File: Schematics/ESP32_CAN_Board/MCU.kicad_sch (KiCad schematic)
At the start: 8 parts, among them U4 ESP32-C3-MINI-1-N4

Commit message: initial design completed
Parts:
- added J1, J2: Screw_Terminal_01x04, TerminalBlock:TerminalBlock_Xinya_XY308-2.54-4P_1x04_P2.54mm_Horizontal, symbol Connector:Screw_Terminal_01x04
- added J3: Screw_Terminal_01x02, TerminalBlock:TerminalBlock_Xinya_XY308-2.54-2P_1x02_P2.54mm_Horizontal, symbol Connector:Screw_Terminal_01x02
- U4: footprint ESP32-C3-MINI-1-N4:XCVR_ESP32-C3-MINI-1-N4 -> myFootprints:XCVR_ESP32-C3-MINI-1-N4
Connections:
- net ESPPower is gone; now on net +3.3V: C1.1, C2.1, U4.3 (3V3)
- net Pin12: now reaches U4.12 (IO0)
- net Pin12: now also J2.2 (Pin_2)
- net Pin13: now reaches U4.13 (IO1)
- net Pin13: now also J2.3 (Pin_3)
- net Pin16: now reaches U4.16 (IO10)
- net Pin16: now also J2.4 (Pin_4)
- net Pin18: now reaches U4.18 (IO4)
- net Pin18: now also J1.1 (Pin_1)
- net at U4.21 (IO7): now also J1.2 (Pin_2)
- net at U4.22 (IO8): now also J1.3 (Pin_3)
- net at U4.23 (IO9): now also J1.4 (Pin_4)
- net at U4.30 (RXD0): now also J3.2 (Pin_2)
- net at U4.31 (TXD0): now also J3.1 (Pin_1)
- net Pin6: now reaches U4.6 (IO3)
- net Pin6: now also J2.1 (Pin_1)
- no-connect marks 12 -> 4
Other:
- moved on the sheet: C1, C2

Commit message: finished ready for order
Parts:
- J1, J2: LCSC (none) -> C915913
- J3: LCSC (none) -> C557685
- R5: LCSC C96346 -> C84376
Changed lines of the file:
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@@
+			)
+		)
+		(property "LCSC" "C915913"
+			(at 95.25 78.74 0)
+			(hide yes)
+			(show_name no)
+			(do_not_autoplace no)
+			(effects
+				(font
+					(size 1.27 1.27)
+				)
 			)
 		)
@@
 			)
 		)
+		(property "LCSC" "C915913"
+			(at 204.47 88.9 0)
+			(hide yes)
+			(show_name no)
+			(do_not_autoplace no)
+			(effects
+				(font
+					(size 1.27 1.27)
+				)
+			)
+		)
 		(pin "2"
 		)
@@
 			)
 		)
-		(property "LCSC" "C96346"
+		(property "LCSC" "C84376"
 			(at 44.45 116.84 90)
 			(hide yes)
@@
 			(at 97.79 109.22 0)
 			(hide yes)
+			(show_name no)
+			(do_not_autoplace no)
+			(effects
+				(font
+					(size 1.27 1.27)
+				)
+			)
+		)
+		(property "LCSC" " C557685"
+			(at 97.79 109.22 0)
+			(hide yes)

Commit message: mcu schematic update
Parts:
- added PowerLED1: RLED, LED_SMD:LED_0603_1608Metric_Pad1.05x0.95mm_HandSolder, symbol Device:LED
- added R7: 1k, Resistor_SMD:R_0805_2012Metric_Pad1.20x1.40mm_HandSolder, symbol Device:R
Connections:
- net +3.3V: now also R7.2
- net GND: now also PowerLED1.1 (K)
- new net: PowerLED1.2 (A), R7.1

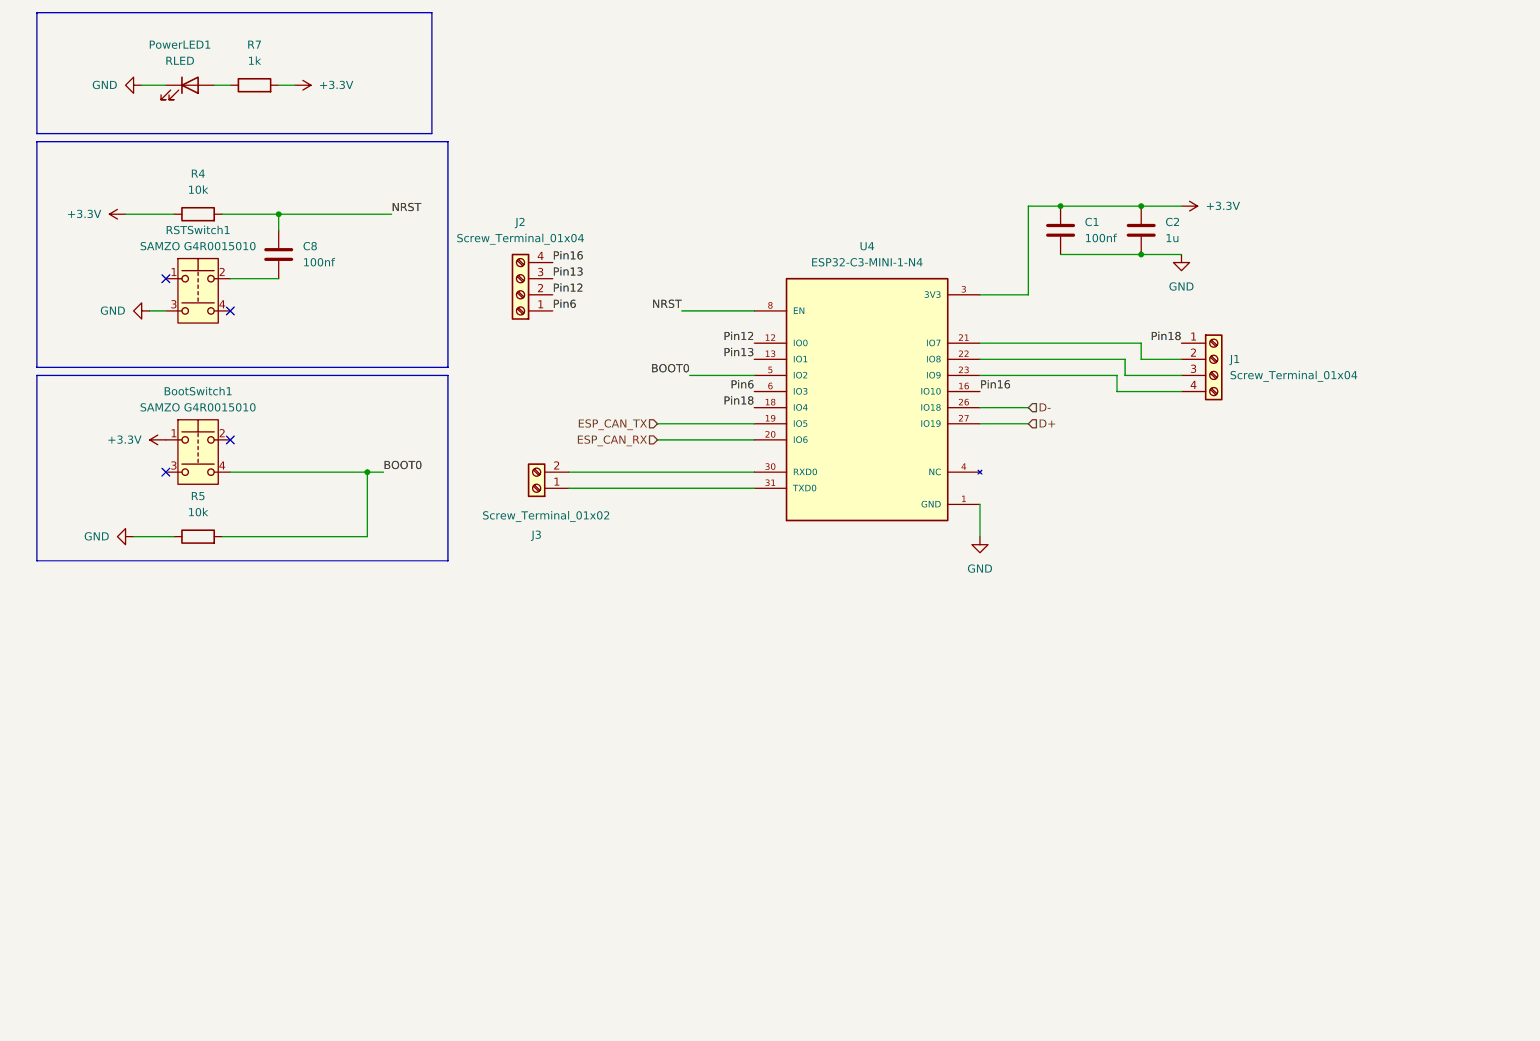
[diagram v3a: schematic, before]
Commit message: final Draft Completed, In JLPCB Cart
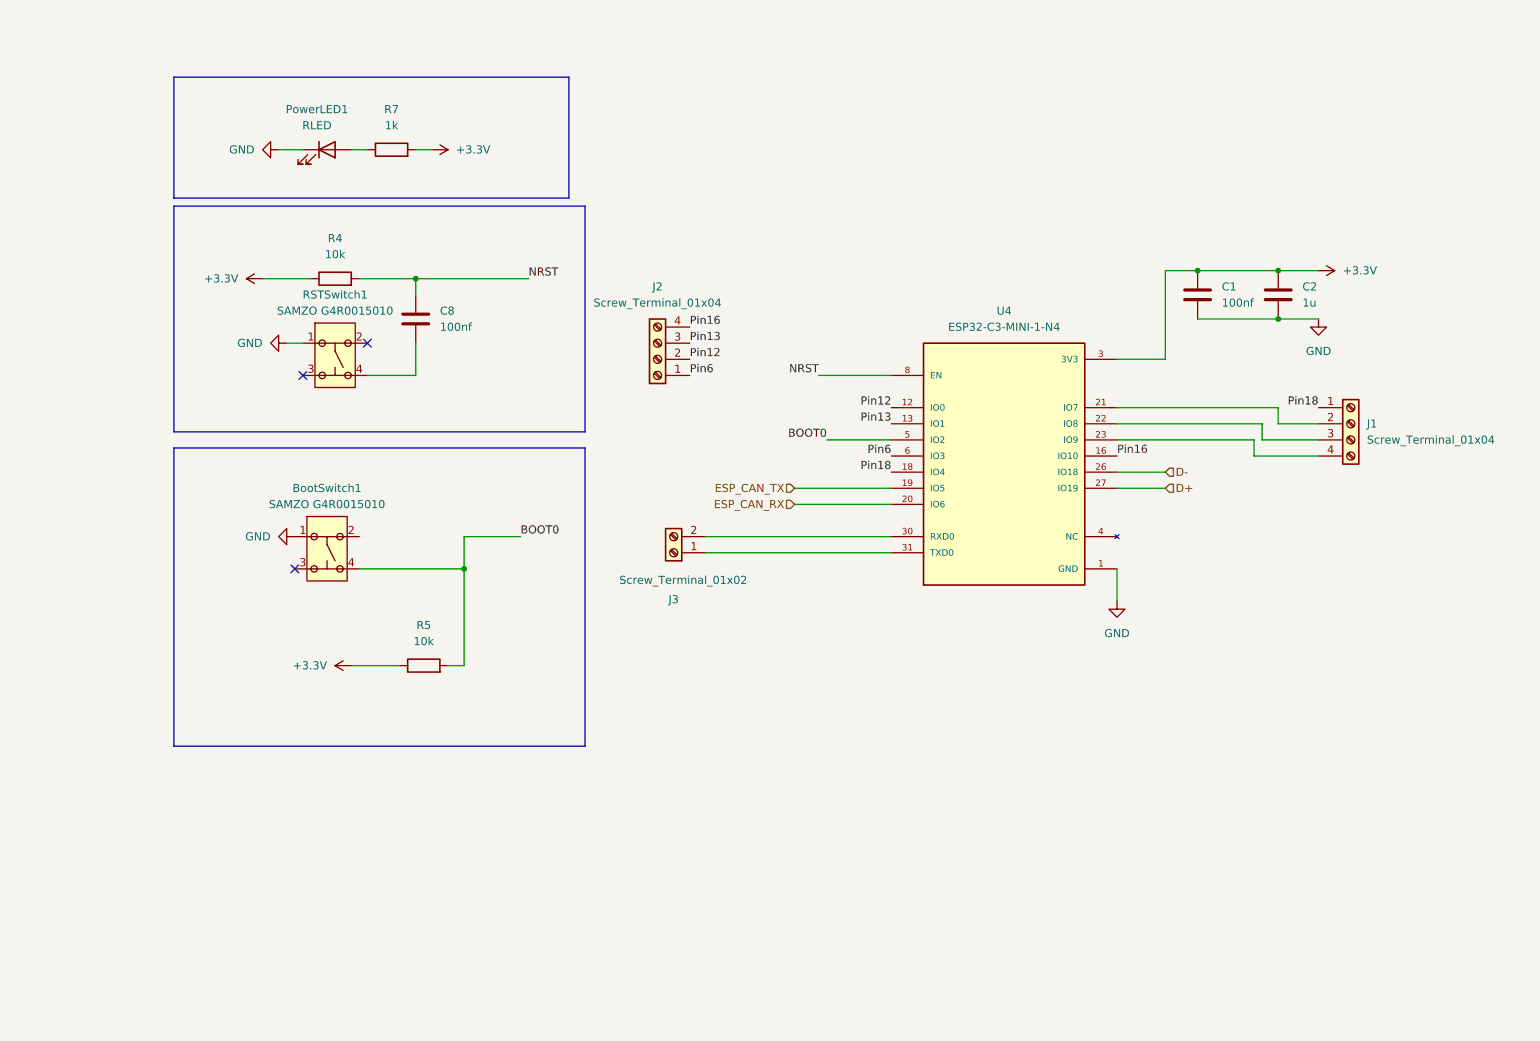
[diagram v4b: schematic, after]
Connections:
- net +3.3V: now also R5.1; no longer BootSwitch1.1
- net GND: now also BootSwitch1.1, RSTSwitch1.1; no longer R5.1, RSTSwitch1.3
- net at RSTSwitch1.2: no longer C8.2
- net at RSTSwitch1.4: now also C8.2
- no-connect marks 4 -> 3
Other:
- moved on the sheet: C1, C2, C8, J1, J2, J3, PowerLED1, R4, R5, R7, U4

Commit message: updated ESPBoard
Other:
- moved on the sheet: BootSwitch1, C1, C2, C8, J1, J2, J3, PowerLED1, R4, R5, R7, RSTSwitch1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
